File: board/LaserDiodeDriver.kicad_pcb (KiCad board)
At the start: 2 copper layers, 55 parts, among them J1 Conn_01x02, K1 EE2-12NU, Q1 2N7002, Q2 IRF9Z34, SW1 SW_SPDT, U1 LT1009, U2 OPA4192, U3 LM317_TO-220

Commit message: Imported power connector models and info.
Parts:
- removed C5: 0.068uF, Capacitor_SMD:C_0603_1608Metric
- added C3: 1uF, Capacitor_SMD:C_0603_1608Metric, F.Cu at (181.7, 103.5)
- J1: footprint Connector_Hirose:Hirose_DF13-02P-1.25DS_1x02_P1.25mm_Horizontal -> Connector_JST:JST_EH_S2B-EH_1x02_P2.50mm_Horizontal
- moved TP5 32.0 mm to (188.5, 112.0)
- moved J1 3.55 mm to (193.5, 100.2), turned to -90 degrees
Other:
- board outline added: 86 x 79 mm

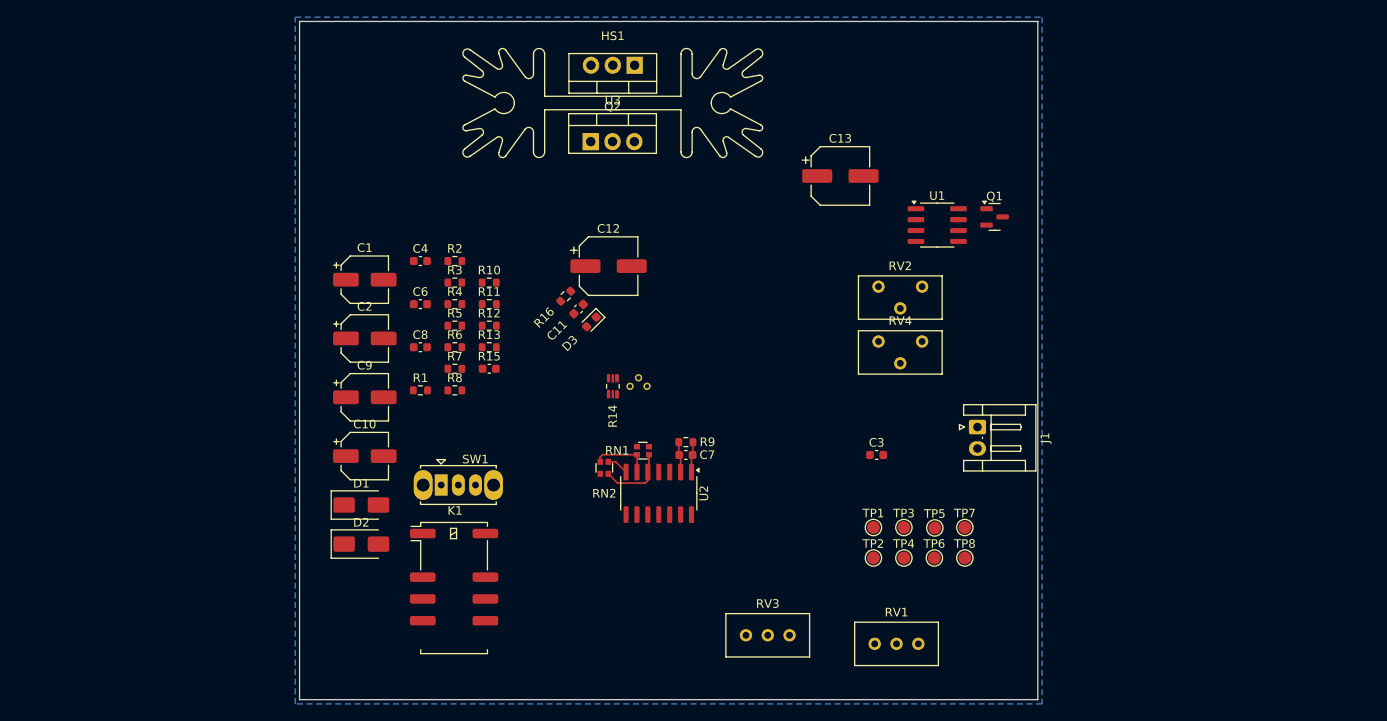
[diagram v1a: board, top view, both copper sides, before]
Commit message: Layout of differential amplifier, TIA, and laser diode.
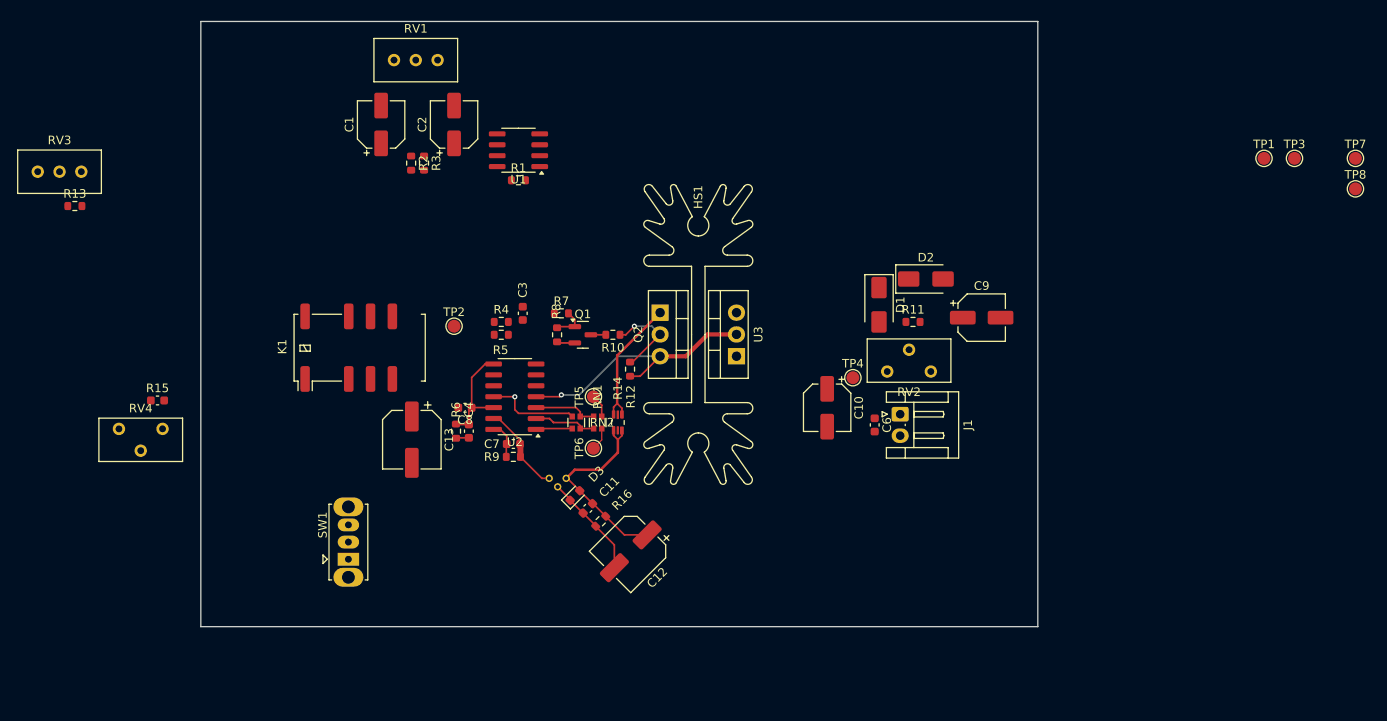
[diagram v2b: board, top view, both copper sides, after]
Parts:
- U3: value LM317_TO-220 -> LM317
- moved RV3 98.6 mm to (89.1, 70.5)
- moved RV4 89.1 mm to (98.5, 100.5)
- moved RV1 88.1 mm to (130.6, 57.5)
- moved D2 72.7 mm to (187.5, 83.0)
- moved C9 72.5 mm to (194.0, 87.5)
- moved D1 64.7 mm to (182.0, 86.0), turned to -90 degrees
- moved TP1 62.6 mm to (226.8, 69.0)
- moved TP3 62.6 mm to (230.4, 69.0)
- moved TP7 62.6 mm to (237.5, 69.0)
- moved TP8 62.6 mm to (237.5, 72.5)
- moved C13 58.6 mm to (127.6, 101.7), turned to -90 degrees
- moved TP2 55.8 mm to (132.5, 88.5)
- moved C6 54.8 mm to (181.5, 100.0), turned to -90 degrees
- moved C10 54.2 mm to (176.0, 98.0), turned to -90 degrees
- moved R13 51.0 mm to (88.3, 74.5)
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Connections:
- C1 pad 1: Net-(U2D-+) -> Net-(U2C-+)
- C13 pad 1: Net-(U2C-+) -> Net-(U2B-+)
- C3 pad 1: Net-(U2C--) -> Net-(U2B--)
- C4 pad 1: Net-(U2D--) -> Net-(U2C--)
- C7 pad 2: Net-(U2A--) -> Net-(U2D--)
- LD1 pad 1: Net-(U2A--) -> Net-(U2D--)
- R14 pad 2: Net-(RN1A-R1.2) -> Net-(RN1B-R2.1)
- R14 pad 3: Net-(RN1B-R2.1) -> Net-(RN1A-R1.2)
- R2 pad 2: Net-(U2D-+) -> Net-(U2C-+)
- R4 pad 2: Net-(U2C--) -> Net-(U2B--)
- R5 pad 2: Net-(U2C-+) -> Net-(U2B-+)
- R6 pad 1: Net-(U2D--) -> Net-(U2C--)
- R9 pad 2: Net-(U2A--) -> Net-(U2D--)
- RN2 pad 2: Net-(RN1B-R2.2) -> Net-(RN1A-R1.1)
- RN2 pad 3: GND -> Net-(RN1B-R2.2)
- RN2 pad 4: Net-(RN1A-R1.1) -> GND
- TP5 pad 1: Net-(RN1A-R1.2) -> Net-(RN1B-R2.1)
- TP6 pad 1: Net-(RN1B-R2.1) -> Net-(RN1A-R1.2)
- U2 pad 1: V_{P_PD} -> V_{I_LD}
- U2 pad 12: Net-(U2D-+) -> v_{ref}
- U2 pad 14: v_{ref} -> V_{P_PD}
- U2 pad 2: Net-(U2A--) -> Net-(RN1A-R1.1)
- U2 pad 3: v_{ref} -> Net-(RN1B-R2.2)
- U2 pad 5: Net-(RN1A-R1.1) -> Net-(U2B-+)
- U2 pad 6: Net-(RN1B-R2.2) -> Net-(U2B--)
- U2 pad 7: V_{I_LD} -> Net-(C3-Pad2)
- U2 pad 8: Net-(C3-Pad2) -> v_{ref}
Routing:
- net +10V: track 0.00 -> 30.8 mm, vias 0 -> 1
- net GND: track 0.00 -> 25.3 mm, vias 0 -> 1
- net Net-(D3-A2): track 0.00 -> 23.5 mm
- net Net-(Q2-D): track 0.00 -> 15.6 mm
- net v_{ref}: track 0.00 -> 12.9 mm
- net Net-(U2D--): track 0.00 -> 10.5 mm
- net Net-(Q2-G): track 0.00 -> 10.3 mm, vias 0 -> 1
- net Net-(Q1-G): track 0.00 -> 4.14 mm
- net Net-(U2A--): track 3.58 -> 0.00 mm
- net Net-(RN1B-R2.1): track 0.00 -> 2.70 mm
- net Net-(RN1A-R1.2): track 0.00 -> 2.70 mm
- net Net-(Q1-D): track 0.00 -> 1.74 mm
- net V_{I_LD}: track 2.56 -> 4.25 mm
- net Net-(U2C--): track 0.00 -> 1.52 mm
- net Net-(RN1A-R1.1): track 8.22 -> 7.38 mm
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- removed copper zone on B.Cu, net GND
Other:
- board size 86 x 79 mm -> 97.5 x 70.5 mm

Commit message: Added laser diode 3D file and more layout
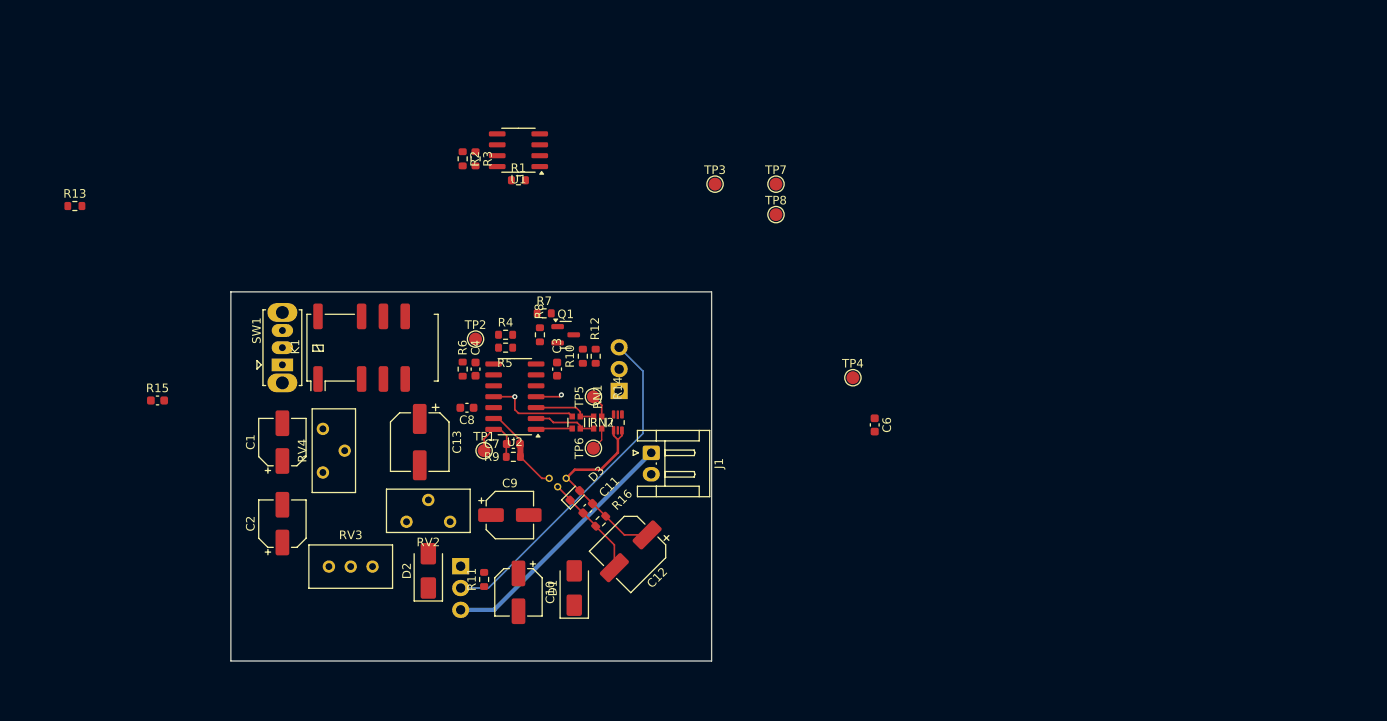
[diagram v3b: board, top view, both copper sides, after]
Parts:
- removed HS1: Heatsink, Heatsink:Heatsink_AAVID_Extruded_531002B00000G_34.9x12.7mm_H25.4mm
- removed RV1: 10k, Potentiometer_THT:Potentiometer_Bourns_3296W_Vertical
- Q2, U3: footprint Package_TO_SOT_THT:TO-220-3_Vertical -> Package_TO_SOT_THT:TO-220-3_Horizontal_TabUp; moved to B.Cu
- moved TP1 97.0 mm to (136.0, 103.0)
- moved TP3 67.6 mm to (162.9, 72.0)
- moved TP7 67.6 mm to (170.0, 72.0)
- moved TP8 67.6 mm to (170.0, 75.5)
- moved D2 67.2 mm to (129.5, 117.0), turned to 90 degrees
- moved C9 59.6 mm to (139.0, 110.5)
- moved RV2 58.7 mm to (127.0, 111.3)
- moved R11 58.3 mm to (136.0, 118.0), turned to 90 degrees
- moved RV3 57.2 mm to (123.0, 116.5)
- moved C2 50.6 mm to (112.5, 111.5)
- moved D1 48.5 mm to (146.5, 119.0), turned to 90 degrees
- moved C10 41.9 mm to (140.0, 119.5)
- moved U3 40.4 mm to (133.3, 116.5), turned to -90 degrees
- moved C1 38.7 mm to (112.5, 102.0)
- moved J1 29.3 mm to (155.5, 103.2)
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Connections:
- U1 pad 5: Net-(U1-FB) -> unconnected-(U1-FB-Pad5)
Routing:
- net +12V: track 0.00 -> 29.8 mm
- net Net-(Q2-D): track 15.6 -> 0.00 mm
- net v_{ref}: track 12.9 -> 0.00 mm
- net +10V: track 30.8 -> 42.9 mm
- net Net-(Q2-G): track 10.3 -> 0.00 mm, vias 1 -> 0
- net Net-(Q1-G): track 4.14 -> 0.00 mm
- net V_{P_PD}: track 4.31 -> 7.24 mm
- net GND: track 25.3 -> 23.2 mm
- net Net-(Q1-D): track 1.74 -> 0.00 mm
- net Net-(U2C--): track 1.52 -> 0.00 mm
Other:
- board size 97.5 x 70.5 mm -> 56 x 43 mm

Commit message: Various changes + component placement
* Removed signal relay in favor of SPDT switch in the interest of space.
* Placed components for optimal mechanical mounting with LD in center of PCB.
* Got rid of LM317 pot for space calculated proper values for LM317 to be +10V output.
* Arranged resistors for good placement.
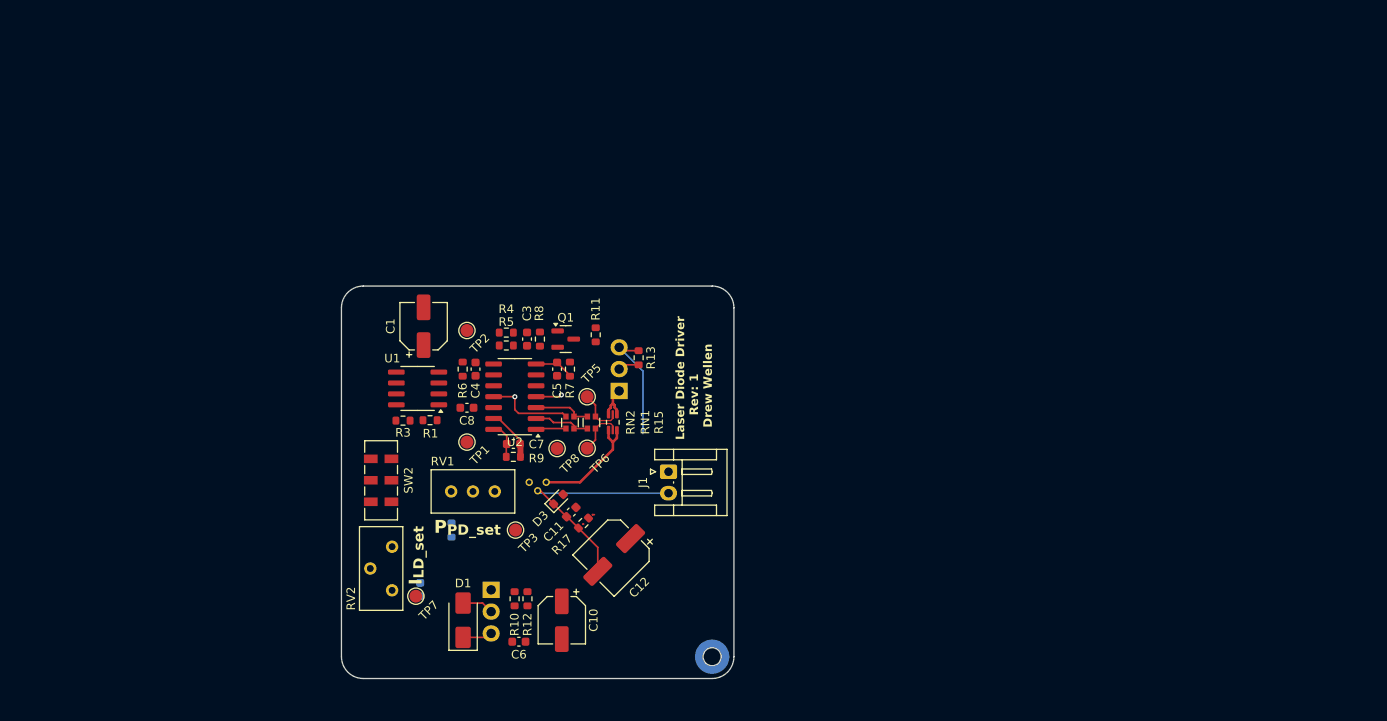
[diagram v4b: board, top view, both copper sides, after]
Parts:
- removed C13: 100uF, Capacitor_SMD:CP_Elec_6.3x5.8
- removed C2, C9: 22uF, Capacitor_SMD:CP_Elec_5x5.8
- removed D2: US2AA, Diode_SMD:D_SMA
- removed K1: EE2-12NU, Relay_SMD:Relay_DPDT_Kemet_EE2_NU
- removed R2: 10k, Resistor_SMD:R_0603_1608Metric
- removed RV3: 10k, Potentiometer_THT:Potentiometer_Bourns_3296W_Vertical
- removed RV4: 5k, Potentiometer_THT:Potentiometer_Bourns_3296Y_Vertical
- removed SW1: SW_SPDT, Button_Switch_THT:SW_Slide_SPDT_Straight_CK_OS102011MS2Q
- removed TP4: +10V, TestPoint:TestPoint_Pad_D1.5mm
- added C5: 1uF, Capacitor_SMD:C_0603_1608Metric, F.Cu at (144.5, 93.5)
- added H1: MountingHole, Mounting_Wuerth:Mounting_Wuerth_WA-SMSI-M1.6_H5mm_ThreadDepth2mm_97730506334, B.Cu at (162.6, 127.0)
- added R17: 100k, Resistor_SMD:R_0603_1608Metric, F.Cu at (147.6, 111.4)
- added RV1: 10k, Potentiometer_THT:Potentiometer_Bourns_3296W_Vertical, F.Cu at (132.2, 107.8)
- added SW2: SW_DPDT_x2, Button_Switch_SMD:SW_DPDT_CK_JS202011JCQN, F.Cu at (124.0, 106.5)
- R10: value 100 -> 2.1k
- R11: value 220 -> 100
- R12: value 100k -> 300
- R13: value 0 -> 100k
- R14: value 1Ω±0.25%, 1/8W -> 0; footprint LD_Library:R_Shunt_0805_2012Metric -> Resistor_SMD:R_0603_1608Metric; moved to B.Cu
- R15: value 68k -> 1Ω±0.25%, 1/8W; footprint Capacitor_SMD:C_0603_1608Metric -> LD_Library:R_Shunt_0805_2012Metric
- R16: value 100k -> 68k; footprint Resistor_SMD:R_0603_1608Metric -> Capacitor_SMD:C_0603_1608Metric; moved to B.Cu
- R5: value 10k -> 100k
- moved R13 68.0 mm to (154.0, 92.2), turned to -90 degrees
- moved TP7 63.7 mm to (128.1, 120.0), turned to 180 degrees
- moved R15 53.1 mm to (151.0, 99.7), turned to -90 degrees
- moved C6 48.5 mm to (140.1, 125.2), turned to 0 degrees
- moved TP3 46.5 mm to (139.7, 112.2)
- moved TP8 37.3 mm to (144.5, 102.7)
- moved R3 31.6 mm to (126.5, 99.5), turned to 0 degrees
- moved R11 31.3 mm to (149.0, 89.5), turned to -90 degrees
- moved U1 30.1 mm to (128.2, 95.8)
- moved R1 29.8 mm to (129.7, 99.5)
- moved R10 29.3 mm to (139.6, 120.2)
- moved R12 29.3 mm to (141.1, 120.2), turned to 90 degrees
- moved R14 23.1 mm to (132.2, 112.2)
- moved R16 22.5 mm to (128.6, 119.2), turned to -90 degrees
- moved C1 21.3 mm to (128.9, 88.5)
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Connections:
- C1 pad 2: Net-(C1-Pad2) -> GND
- C3 pad 1: Net-(U2B--) -> GND
- C3 pad 2: Net-(C3-Pad2) -> Net-(U2B-+)
- R10 pad 1: Net-(Q1-D) -> Net-(U3-ADJ)
- R10 pad 2: Net-(Q2-G) -> GND
- R11 pad 1: +10V -> Net-(Q1-D)
- R11 pad 2: Net-(D2-A) -> Net-(Q2-G)
- R12 pad 2: Net-(Q2-G) -> Net-(U3-ADJ)
- R13 pad 2: Net-(R13-Pad2) -> Net-(Q2-G)
- R14 pad 1: Net-(Q2-D) -> +10V
- R14 pad 2: Net-(RN1B-R2.1) -> Net-(R14-Pad2)
- R15 pad 1: v_{ref} -> Net-(Q2-D)
- R15 pad 2: Net-(R15-Pad2) -> Net-(RN1B-R2.1)
- R16 pad 1: Net-(D3-A2) -> v_{ref}
- R16 pad 2: GND -> Net-(R16-Pad2)
- R3 pad 2: Net-(C1-Pad2) -> Net-(U2C-+)
- R7 pad 1: Net-(C3-Pad2) -> Net-(C5-Pad2)
- RV2 pad 1: Net-(D2-A) -> Net-(R16-Pad2)
- RV2 pad 2: GND -> I_{LD_set}
- U2 pad 7: Net-(C3-Pad2) -> Net-(C5-Pad2)
- U3 pad 1: Net-(D2-A) -> Net-(U3-ADJ)
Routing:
- net +12V: track 29.8 -> 3.46 mm
- net +10V: track 42.9 -> 20.3 mm
- net GND: track 23.2 -> 38.7 mm
- net Net-(D3-A2): track 23.5 -> 13.6 mm
- net Net-(C5-Pad2): track 0.00 -> 4.74 mm
- net Net-(Q2-D): track 0.00 -> 4.68 mm
- net Net-(U2D--): track 10.5 -> 6.10 mm
- net V_{P_PD}: track 7.24 -> 4.31 mm
- net Net-(RN1A-R1.2): track 2.70 -> 5.58 mm
- net Net-(RN1B-R2.1): track 2.70 -> 5.48 mm
- net Net-(Q2-G): track 0.00 -> 2.48 mm
- net Net-(RN1B-R2.2): track 7.46 -> 6.73 mm
- net Net-(RN1A-R1.1): track 7.38 -> 6.65 mm
- net V_{I_LD}: track 4.25 -> 3.52 mm
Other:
- board size 56 x 43 mm -> 45.7 x 45.7 mm
- board text added: "I_{LD_set}"
- board text added: "Laser Diode Driver Rev: 1 Drew Wellen"
- board text added: "P_{PD_set}"
